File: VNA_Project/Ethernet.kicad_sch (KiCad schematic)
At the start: 0 parts

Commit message: minor changes eth
minor changes eth
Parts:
- added J1001: RJ45_Wuerth_7499010211A, Connector_RJ:RJ45_Wuerth_7499010211A_Horizontal, symbol Connector:RJ45_Wuerth_7499010211A
- added U1001: DP83848C, Package_QFP:LQFP-48_7x7mm_P0.5mm, symbol Interface_Ethernet:DP83848C
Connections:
- new net +3.3V: U1001.32 (IOVDD33), U1001.48 (IOVDD33)
- new net +3.3VA: U1001.22 (AVDD33)
- new net ETH_CRS_DV: U1001.40 (CRS/CRS_DV/LED_CFG)
- new net ETH_MDIO: U1001.30 (MDIO)
- new net ETH_RXD0: U1001.43 (RXD_0/PHY_AD1)
- new net ETH_RXD1: U1001.44 (RXD_1/PHY_AD2)
- new net ETH_RX_CLK: U1001.38 (RX_CLK)
- new net ETH_TXD0: U1001.3 (TXD_0)
- new net ETH_TXD1: U1001.4 (TXD_1)
- new net ETH_TX_EN: U1001.2 (TX_EN)
- new net GND: U1001.15 (AGND), U1001.19 (AGND), U1001.35 (IOGND), U1001.36 (DGND), U1001.47 (IOGND)
- new net NRST: U1001.29 (~{RESET})

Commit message: eth
eth
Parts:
- added C1001, C1002, C1004: 0.1u, symbol Device:C_Small
- added C1003: 10u, symbol Device:C_Small
- added C1005, C1006: 0.1u, symbol Device:C
- added D1001: RED, symbol Device:LED
- added D1002: GREEN, symbol Device:LED
- added D1003: BLUE, symbol Device:LED
- added FL1001, FL1002: Choke_CommonMode_PulseElectronics_PH9455x105NL, Inductor_THT:L_CommonMode_PulseElectronics_PH9455x105NL_1, symbol Filter:Choke_CommonMode_PulseElectronics_PH9455x105NL
- added R1001: 1.5k, symbol Device:R
- added R1002: 4.87k, symbol Device:R
- added R1003, R1004: 2.2k, symbol Device:R
- added R1005, R1006, R1007: 1k, symbol Device:R
- added R1008, R1009, R1010, R1011: 49.9, symbol Device:R
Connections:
- net +3.3V: now also C1005.1, C1006.1, R1001.1, R1008.2, R1009.1, R1010.2, R1011.1
- net +3.3VA: now also R1003.2, R1004.2
- net ETH_MDIO: now also R1001.2
- net GND: now also C1001.2, C1002.2, C1003.2, C1004.2, C1005.2, C1006.2, R1002.2, R1005.2, R1006.2, R1007.2
- net RD-: now reaches U1001.13 (RD-)
- net RD-: now also FL1002.2, R1011.2
- net RD+: now reaches U1001.14 (RD+)
- net RD+: now also FL1002.1, R1010.1
- net TD-: now reaches U1001.16 (TD-)
- net TD-: now also FL1001.2, R1009.2
- net TD+: now reaches U1001.17 (TD+)
- net TD+: now also FL1001.1, R1008.1
- net at U1001.18 (PFBIN1): now also U1001.23 (PFBOUT), U1001.37 (PFBIN2), C1001.1, C1002.1, C1003.1, C1004.1
- net at U1001.20 (RESERVED): now also R1003.1
- net at U1001.21 (RESERVED): now also R1004.1
- net at U1001.24 (RBIAS): now also R1002.1
- net LED_ACT: now reaches U1001.26 (AN_EN/LED_ACT/COL)
- net LED_ACT: now also D1003.2 (A)
- net LED_SPEED: now reaches U1001.27 (AN1/LED_SPEED)
- net LED_SPEED: now also D1002.2 (A)
- net LED_LINK: now reaches U1001.28 (AN0/LED_LINK)
- net LED_LINK: now also D1001.2 (A)
- new net: D1001.1 (K), R1005.1
- new net: D1002.1 (K), R1006.1
- new net: D1003.1 (K), R1007.1
- no-connect marks 0 -> 2
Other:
- note added: "1%"
- note added: "RMII Mode"
- note added: "Status LEDs"
- note added: "tantalum"
- moved on the sheet: J1001, U1001

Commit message: Eth done
Eth done
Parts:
- removed C1001, C1002, C1004: 0.1u, symbol Device:C_Small
- removed C1003: 10u, symbol Device:C_Small
- removed C1005, C1006: 0.1u, symbol Device:C
- removed D1001: RED, symbol Device:LED
- removed D1002: GREEN, symbol Device:LED
- removed D1003: BLUE, symbol Device:LED
- removed FL1001, FL1002: Choke_CommonMode_PulseElectronics_PH9455x105NL, Inductor_THT:L_CommonMode_PulseElectronics_PH9455x105NL_1, symbol Filter:Choke_CommonMode_PulseElectronics_PH9455x105NL
- removed R1001: 1.5k, symbol Device:R
- removed R1002: 4.87k, symbol Device:R
- removed R1003, R1004: 2.2k, symbol Device:R
- removed R1005, R1006, R1007: 1k, symbol Device:R
- removed R1008, R1009, R1010, R1011: 49.9, symbol Device:R
- removed U1001: DP83848C, Package_QFP:LQFP-48_7x7mm_P0.5mm, symbol Interface_Ethernet:DP83848C
- added C1, C10, C11, C7, C8, C9: 100n, symbol Device:C
- added C2, C3: 5.6p, symbol Device:C
- added C4: 1u, symbol Device:C
- added C5: 470p, symbol Device:C
- added C6: 10u, symbol Device:C
- added L1: 600R @ 100 MHz, symbol Device:L
- added R1: 0, symbol Device:R
- added R10, R12: 270, symbol Device:R
- added R11: 10K, symbol Device:R
- added R13, R14: 33, symbol Device:R_Small
- added R15: 10k, symbol Device:R_Small
- added R16: 12.1k, symbol Device:R_Small
- added R2, R3, R4, R7: 49.9, symbol Device:R
- added TR1: Wuerth_749013011A, Transformer_SMD:Transformer_Ethernet_Wuerth_749013011A, symbol Transformer:Wuerth_749013011A
- added U1: LAN8742A, Package_DFN_QFN:VQFN-24-1EP_4x4mm_P0.5mm_EP2.5x2.5mm_ThermalVias, symbol Interface_Ethernet:LAN8742A
- added U2: USBLC6-4SC6, Package_TO_SOT_SMD:SOT-23-6, symbol Power_Protection:USBLC6-4SC6
- added Y1: NX2016SA25MHz, symbol Device:Crystal_GND24
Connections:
- net +3.3V: now also C1.1, U1.9 (VDDIO)
- net +3.3VA: now also L1.1
- net ETH_CRS_DV: now also U1.11 (CRS_DV/MODE2)
- net ETH_MDIO: now also U1.12 (MDIO)
- net ETH_RXD0: now also R13.1
- net ETH_RXD1: now also R14.1
- net ETH_RX_CLK: now also U1.14 (~{INT}/REFCLKO)
- net ETH_TXD0: now also U1.17 (TXD0)
- net ETH_TXD1: now also U1.18 (TXD1)
- net ETH_TX_EN: now also U1.16 (TXEN)
- net GND: now also J1001.8, J1001.SH, C1.2, C10.2, C11.2, C2.2, C3.2, C4.2, C5.2, C6.2, C7.2, C8.2, C9.2, R10.2, R11.2, R12.2, R15.2, R16.1, U1.25 (VSS), U2.2 (GND), Y1.2, Y1.4
- net NRST: now also U1.15 (~{RST})
- net RD+: now also J1001.3 (RD+), TR1.11 (RX+)
- net RD-: now also J1001.6 (RD-), TR1.9 (RX-)
- net TD+: now also J1001.1 (TD+), TR1.16 (TX+)
- net TD-: now also J1001.2 (TD-), TR1.14 (TX-)
- net at J1001.10: now also R10.1
- net at J1001.11: now also R12.1
- net LED_REGOFF: now reaches J1001.12
- net LED_REGOFF: now also U1.3 (LED1/REGOFF)
- net CRD: now reaches J1001.4 (CTD)
- net CRD: now also TR1.10 (C_RX)
- net CTD: now reaches J1001.5 (CRD)
- net CTD: now also TR1.15 (C_TX)
- net LED_INTSEL: now reaches J1001.9
- net LED_INTSEL: now also R11.1, U1.2 (LED2/~{INTSEL})
- new net: R13.2, U1.8 (RXD0/MODE0)
- new net: R15.1, U1.10 (RXER/PHYAD0)
- new net: R16.2, U1.24 (RBIAS)
- new net: C2.1, R1.1, U1.5 (XTAL1/CLKIN)
- new net: C4.1, C5.1, U1.6 (VDDCR)
- new net: R14.2, U1.7 (RXD1/MODE1)
- new net: R1.2, Y1.1
- new net CT: C10.1, C11.1, C6.1, C7.1, C8.1, C9.1, L1.2, R2.1, R3.1, R4.1, R7.1, TR1.2 (C_TD), TR1.7 (C_RD), U1.1 (VDD2A), U1.19 (VDD1A), U2.5 (VBUS)
- new net ETH_MDC: U1.13 (MDC)
- new net RX+: R4.2, TR1.6 (RD+), U1.23 (RXP), U2.1 (I/O1)
- new net RX-: R7.2, TR1.8 (RD-), U1.22 (RXN), U2.6 (I/O4)
- new net TX+: R2.2, TR1.1 (TD+), U1.21 (TXP), U2.3 (I/O2)
- new net TX-: R3.2, TR1.3 (TD-), U1.20 (TXN), U2.4 (I/O3)
- new net xtal2_eth: C3.1, U1.4 (XTAL2), Y1.3
- no-connect marks 2 -> 0
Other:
- note added: "25MHZ"
- note added: "Connector"
- note added: "ESD"
- note added: "MAGNETICS"
- note added: "PHY"
- note removed: "1%"
- note removed: "Status LEDs"
- note removed: "tantalum"
- moved on the sheet: J1001

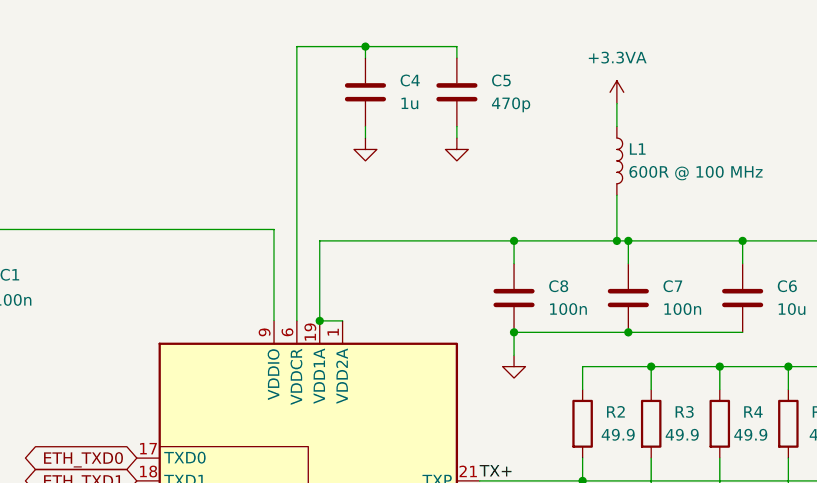
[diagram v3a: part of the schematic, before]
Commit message: finishing up front end
refining Non RF front end
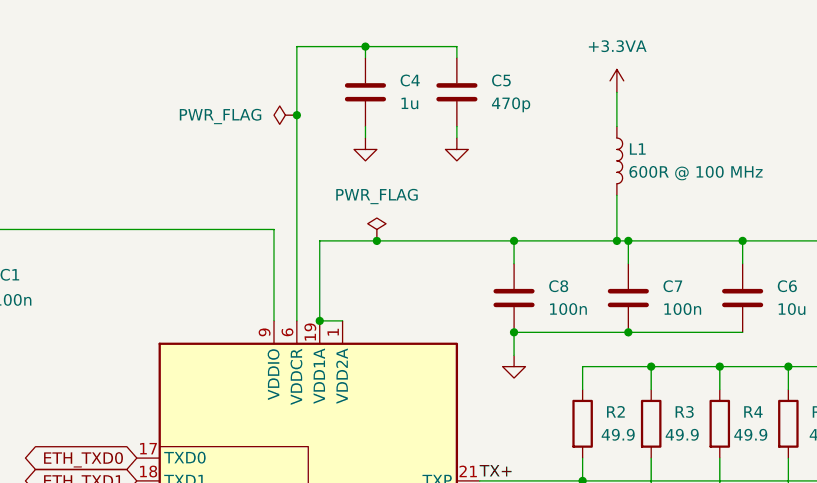
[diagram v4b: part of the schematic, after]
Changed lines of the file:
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@@
 	)
 	(junction
+		(at 125.73 22.86)
+		(diameter 0)
+		(color 0 0 0 0)
+	)
+	(junction
 		(at 162.56 36.83)
 		(diameter 0)
@@
 	)
 	(junction
+		(at 134.62 36.83)
+		(diameter 0)
+		(color 0 0 0 0)
+	)
+	(junction
 		(at 165.1 50.8)
 		(diameter 0)
@@
 	(wire
 		(pts
+			(xy 134.62 36.83) (xy 128.27 36.83)
+		)
+		(stroke
+			(width 0)
+			(type default)
+		)
+	)
+	(wire
+		(pts
 			(xy 226.06 140.97) (xy 251.46 140.97)
 		)
@@
 	(wire
 		(pts
+			(xy 125.73 22.86) (xy 125.73 45.72)
+		)
+		(stroke
+			(width 0)
+			(type default)
+		)
+	)
+	(wire
+		(pts
 			(xy 175.26 36.83) (xy 175.26 39.37)
 		)
@@
 	(wire
 		(pts
-			(xy 149.86 36.83) (xy 128.27 36.83)
+			(xy 149.86 36.83) (xy 134.62 36.83)
 		)
 		(stroke
@@
 	(wire
 		(pts
-			(xy 125.73 15.24) (xy 125.73 45.72)
+			(xy 125.73 15.24) (xy 125.73 22.86)
 		)
 		(stroke
@@
 	(wire
 		(pts
-			(xy 161.29 21.59) (xy 161.29 24.13)
+			(xy 161.29 20.32) (xy 161.29 24.13)
 		)
 		(stroke
@@
 	)
 	(symbol
+		(lib_id "power:PWR_FLAG")
+		(at 134.62 36.83 0)
+		(unit 1)
+		(exclude_from_sim no)
+		(in_bom yes)
+		(on_board yes)
+		(dnp no)
+		(fields_autoplaced yes)
+		(property "Reference" "#FLG08"
+			(at 134.62 34.925 0)
+			(effects
+				(font
+					(size 1.27 1.27)
+				)
+				(hide yes)
+			)
+		)
+		(property "Value" "PWR_FLAG"
+			(at 134.62 31.75 0)
+			(effects
+				(font
+					(size 1.27 1.27)
+				)
+			)
+		)
+		(property "Footprint" ""
+			(at 134.62 36.83 0)
+			(effects
+				(font
+					(size 1.27 1.27)
+				)
+				(hide yes)
+			)
+		)
+		(property "Datasheet" "~"
+			(at 134.62 36.83 0)
+			(effects
+				(font
+					(size 1.27 1.27)
+				)
+				(hide yes)
+			)
+		)
+		(property "Description" "Special symbol for telling ERC where power comes from"
+			(at 134.62 36.83 0)
+			(effects
+				(font
+					(size 1.27 1.27)
+				)
+				(hide yes)
+			)
+		)
+		(pin "1"
+		)
+		(instances
+			(project ""
+				(path "/8b9c6944-c5f7-4a92-a452-dc4fa5f3924d/76256ba9-bc22-4fd8-98b4-4441e825b7f8"
+					(reference "#FLG08")
+					(unit 1)
+				)
+			)
+		)
+	)
+	(symbol
 		(lib_id "power:GND")
 		(at 149.86 49.53 0)
@@
 	(symbol
 		(lib_id "power:+3.3VA")
-		(at 161.29 21.59 0)
+		(at 161.29 20.32 0)
 		(unit 1)
 		(exclude_from_sim no)
@@
 		(fields_autoplaced yes)
 		(property "Reference" "#PWR08"
-			(at 161.29 25.4 0)
+			(at 161.29 24.13 0)
 			(effects
 				(font
@@
 		)
 		(property "Value" "+3.3VA"
-			(at 161.29 16.51 0)
+			(at 161.29 15.24 0)
 			(effects
 				(font
@@
 		)
 		(property "Footprint" ""
-			(at 161.29 21.59 0)
+			(at 161.29 20.32 0)
 			(effects
 				(font
@@
 		)
 		(property "Datasheet" ""
-			(at 161.29 21.59 0)
+			(at 161.29 20.32 0)
 			(effects
 				(font
@@
 		)
 		(property "Description" "Power symbol creates a global label with name \"+3.3VA\""
-			(at 161.29 21.59 0)
+			(at 161.29 20.32 0)
 			(effects
 				(font
@@
 					(unit 1)
 				)
+			)
+		)
+	)
+	(symbol
+		(lib_id "power:PWR_FLAG")
+		(at 125.73 22.86 90)
+		(unit 1)
+		(exclude_from_sim no)
+		(in_bom yes)
+		(on_board yes)
+		(dnp no)
+		(fields_autoplaced yes)
+		(property "Reference" "#FLG09"
+			(at 123.825 22.86 0)
+			(effects
+				(font
+					(size 1.27 1.27)
+				)
+				(hide yes)
+			)
+		)
+		(property "Value" "PWR_FLAG"
+			(at 121.92 22.8599 90)
+			(effects
+				(font
+					(size 1.27 1.27)
+				)
+				(justify left)
+			)
+		)
+		(property "Footprint" ""
+			(at 125.73 22.86 0)
+			(effects
+				(font
+					(size 1.27 1.27)
+				)
+				(hide yes)
+			)
+		)
+		(property "Datasheet" "~"
+			(at 125.73 22.86 0)
+			(effects
+				(font
+					(size 1.27 1.27)
+				)
+				(hide yes)
+			)
+		)
+		(property "Description" "Special symbol for telling ERC where power comes from"
+			(at 125.73 22.86 0)
+			(effects
+				(font
+					(size 1.27 1.27)
+				)
+				(hide yes)
+			)
+		)
+		(pin "1"
+		)
+		(instances
+			(project "VNA_Project"
+				(path "/8b9c6944-c5f7-4a92-a452-dc4fa5f3924d/76256ba9-bc22-4fd8-98b4-4441e825b7f8"
+					(reference "#FLG09")
+					(unit 1)
+				)

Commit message: AA filtering
redoing AA filtering
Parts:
- added TP15, TP16: TestPoint, symbol Connector:TestPoint
- C2, C3: value 5.6p -> 10p
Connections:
- net +3.3V: now also TP15.1
- net CT: now also TP16.1
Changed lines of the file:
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@@
 	)
 	(junction
+		(at 128.27 41.91)
+		(diameter 0)
+		(color 0 0 0 0)
+	)
+	(junction
 		(at 218.44 149.86)
 		(diameter 0)
@@
 	)
 	(junction
+		(at 123.19 41.91)
+		(diameter 0)
+		(color 0 0 0 0)
+	)
+	(junction
 		(at 172.72 68.58)
 		(diameter 0)
@@
 	(wire
 		(pts
+			(xy 123.19 41.91) (xy 123.19 45.72)
+		)
+		(stroke
+			(width 0)
+			(type default)
+		)
+	)
+	(wire
+		(pts
 			(xy 157.48 63.5) (xy 157.48 83.82)
 		)
@@
 	(wire
 		(pts
-			(xy 123.19 35.56) (xy 123.19 45.72)
+			(xy 123.19 35.56) (xy 123.19 41.91)
 		)
 		(stroke
@@
 	(wire
 		(pts
-			(xy 157.48 83.82) (xy 203.2 83.82)
-		)
-		(stroke
-			(width 0)
-			(type default)
-		)
-	)
-	(wire
-		(pts
 			(xy 194.31 58.42) (xy 198.12 58.42)
 		)
@@
 	(wire
 		(pts
+			(xy 180.34 99.06) (xy 203.2 99.06)
+		)
+		(stroke
+			(width 0)
+			(type default)
+		)
+	)
+	(wire
+		(pts
 			(xy 196.85 106.68) (xy 196.85 107.95)
 		)
@@
 	(wire
 		(pts
+			(xy 172.72 93.98) (xy 203.2 93.98)
+		)
+		(stroke
+			(width 0)
+			(type default)
+		)
+	)
+	(wire
+		(pts
 			(xy 157.48 50.8) (xy 157.48 53.34)
 		)
@@
 	(wire
 		(pts
-			(xy 128.27 36.83) (xy 128.27 45.72)
+			(xy 128.27 36.83) (xy 128.27 41.91)
 		)
 		(stroke
@@
 	(wire
 		(pts
+			(xy 85.09 93.98) (xy 107.95 93.98)
+		)
+		(stroke
+			(width 0)
+			(type default)
+		)
+	)
+	(wire
+		(pts
 			(xy 146.05 86.36) (xy 146.05 100.33)
 		)
@@
 	(wire
 		(pts
-			(xy 85.09 93.98) (xy 107.95 93.98)
-		)
-		(stroke
-			(width 0)
-			(type default)
-		)
-	)
-	(wire
-		(pts
 			(xy 196.85 60.96) (xy 198.12 60.96)
 		)
@@
 	(wire
 		(pts
+			(xy 157.48 83.82) (xy 203.2 83.82)
+		)
+		(stroke
+			(width 0)
+			(type default)
+		)
+	)
+	(wire
+		(pts
 			(xy 88.9 34.29) (xy 88.9 35.56)
 		)
@@
 	(wire
 		(pts
-			(xy 172.72 93.98) (xy 203.2 93.98)
-		)
-		(stroke
-			(width 0)
-			(type default)
-		)
-	)
-	(wire
-		(pts
 			(xy 196.85 71.12) (xy 196.85 60.96)
 		)
@@
 	(wire
 		(pts
-			(xy 179.07 138.43) (xy 182.88 138.43)
+			(xy 128.27 41.91) (xy 128.27 45.72)
 		)
 		(stroke
@@
 	(wire
 		(pts
-			(xy 180.34 99.06) (xy 203.2 99.06)
+			(xy 179.07 138.43) (xy 182.88 138.43)
 		)
 		(stroke
@@
 	)
 	(symbol
+		(lib_id "Connector:TestPoint")
+		(at 128.27 41.91 270)
+		(unit 1)
+		(exclude_from_sim no)
+		(in_bom yes)
+		(on_board yes)
+		(dnp no)
+		(fields_autoplaced yes)
+		(property "Reference" "TP16"
+			(at 133.35 41.9099 90)
+			(effects
+				(font
+					(size 1.27 1.27)
+				)
+				(justify left)
+			)
+		)
+		(property "Value" "TestPoint"
+			(at 133.35 43.1799 90)
+			(effects
+				(font
+					(size 1.27 1.27)
+				)
+				(justify left)
+				(hide yes)
+			)
+		)
+		(property "Footprint" ""
+			(at 128.27 46.99 0)
+			(effects
+				(font
+					(size 1.27 1.27)
+				)
+				(hide yes)
+			)
+		)
+		(property "Datasheet" "~"
+			(at 128.27 46.99 0)
+			(effects
+				(font
+					(size 1.27 1.27)
+				)
+				(hide yes)
+			)
+		)
+		(property "Description" "test point"
+			(at 128.27 41.91 0)
+			(effects
+				(font
+					(size 1.27 1.27)
+				)
+				(hide yes)
+			)
+		)
+		(pin "1"
+		)
+		(instances
+			(project "VNA_Project"
+				(path "/8b9c6944-c5f7-4a92-a452-dc4fa5f3924d/76256ba9-bc22-4fd8-98b4-4441e825b7f8"
+					(reference "TP16")
+					(unit 1)
+				)
+			)
+		)
+	)
+	(symbol
 		(lib_id "Device:C")
 		(at 175.26 43.18 0)
@@
 	)
 	(symbol
+		(lib_id "Connector:TestPoint")
+		(at 123.19 41.91 90)
+		(unit 1)
+		(exclude_from_sim no)
+		(in_bom yes)
+		(on_board yes)
+		(dnp no)
+		(fields_autoplaced yes)
+		(property "Reference" "TP15"
+			(at 119.888 39.37 90)
+			(effects
+				(font
+					(size 1.27 1.27)
+				)
+			)
+		)
+		(property "Value" "TestPoint"
+			(at 118.11 40.6401 90)
+			(effects
+				(font
+					(size 1.27 1.27)
+				)
+				(justify left)
+				(hide yes)
+			)
+		)
+		(property "Footprint" ""
+			(at 123.19 36.83 0)
+			(effects
+				(font
+					(size 1.27 1.27)
+				)
+				(hide yes)
+			)
+		)
+		(property "Datasheet" "~"
+			(at 123.19 36.83 0)
+			(effects
+				(font
+					(size 1.27 1.27)
+				)
+				(hide yes)
+			)
+		)
+		(property "Description" "test point"
+			(at 123.19 41.91 0)
+			(effects
+				(font
+					(size 1.27 1.27)
+				)
+				(hide yes)
+			)
+		)
+		(pin "1"
+		)
+		(instances
+			(project "VNA_Project"
+				(path "/8b9c6944-c5f7-4a92-a452-dc4fa5f3924d/76256ba9-bc22-4fd8-98b4-4441e825b7f8"
+					(reference "TP15")
+					(unit 1)
+				)
+			)
+		)
+	)
+	(symbol
 		(lib_id "Device:C")
 		(at 182.88 111.76 0)
@@
 		(fields_autoplaced yes)
 		(property "Reference" "C3"
-			(at 36.83 100.3299 0)
+			(at 44.45 100.3299 0)
 			(effects
 				(font
 					(size 1.27 1.27)
 				)
-				(justify left)
+				(justify right)
 			)
 		)
-		(property "Value" "5.6p"
-			(at 36.83 102.8699 0)
+		(property "Value" "10p"
+			(at 44.45 102.8699 0)
 			(effects
 				(font
 					(size 1.27 1.27)
 				)
-				(justify left)
+				(justify right)
 			)
 		)
@@
 		(fields_autoplaced yes)
 		(property "Reference" "C2"
-			(at 81.28 100.3299 0)
+			(at 88.9 100.3299 0)
 			(effects
 				(font
 					(size 1.27 1.27)
 				)
-				(justify left)
+				(justify right)
 			)
 		)
-		(property "Value" "5.6p"
-			(at 81.28 102.8699 0)
+		(property "Value" "10p"
+			(at 88.9 102.8699 0)
 			(effects
 				(font
 					(size 1.27 1.27)
 				)
-				(justify left)
+				(justify right)
 			)
 		)

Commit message: footprints + initial layout shape
footprints + initial layout shape
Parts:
- C501: renamed from C3; footprint (none) -> Capacitor_SMD:C_0603_1608Metric_Pad1.08x0.95mm_HandSolder
- C502: renamed from C2; footprint (none) -> Capacitor_SMD:C_0603_1608Metric_Pad1.08x0.95mm_HandSolder
- C503: renamed from C1; footprint (none) -> Capacitor_SMD:C_0603_1608Metric_Pad1.08x0.95mm_HandSolder
- C504: renamed from C4; footprint (none) -> Capacitor_SMD:C_0603_1608Metric_Pad1.08x0.95mm_HandSolder
- C505: renamed from C5; footprint (none) -> Capacitor_SMD:C_0603_1608Metric_Pad1.08x0.95mm_HandSolder
- C506: renamed from C8; footprint (none) -> Capacitor_SMD:C_0603_1608Metric_Pad1.08x0.95mm_HandSolder
- C507: renamed from C7; footprint (none) -> Capacitor_SMD:C_0603_1608Metric_Pad1.08x0.95mm_HandSolder
- C508: renamed from C6; footprint (none) -> Capacitor_SMD:C_0603_1608Metric_Pad1.08x0.95mm_HandSolder
- C509: renamed from C10; footprint (none) -> Capacitor_SMD:C_0603_1608Metric_Pad1.08x0.95mm_HandSolder
- C510: renamed from C11; footprint (none) -> Capacitor_SMD:C_0603_1608Metric_Pad1.08x0.95mm_HandSolder
- C511: renamed from C9; footprint (none) -> Capacitor_SMD:C_0603_1608Metric_Pad1.08x0.95mm_HandSolder
- L501: renamed from L1; footprint (none) -> Inductor_SMD:L_0805_2012Metric_Pad1.15x1.40mm_HandSolder
- R501: renamed from R1; footprint (none) -> Resistor_SMD:R_0603_1608Metric_Pad0.98x0.95mm_HandSolder
- R502: renamed from R13; footprint (none) -> Resistor_SMD:R_0603_1608Metric_Pad0.98x0.95mm_HandSolder
- R503: renamed from R14; footprint (none) -> Resistor_SMD:R_0603_1608Metric_Pad0.98x0.95mm_HandSolder
- R504: renamed from R15; footprint (none) -> Resistor_SMD:R_0603_1608Metric_Pad0.98x0.95mm_HandSolder
- R505: renamed from R16; footprint (none) -> Resistor_SMD:R_0603_1608Metric_Pad0.98x0.95mm_HandSolder
- R506: renamed from R2; footprint (none) -> Resistor_SMD:R_0603_1608Metric_Pad0.98x0.95mm_HandSolder
- R507: renamed from R3; footprint (none) -> Resistor_SMD:R_0603_1608Metric_Pad0.98x0.95mm_HandSolder
- R508: renamed from R4; footprint (none) -> Resistor_SMD:R_0603_1608Metric_Pad0.98x0.95mm_HandSolder
- R509: renamed from R7; footprint (none) -> Resistor_SMD:R_0603_1608Metric_Pad0.98x0.95mm_HandSolder
- R510: renamed from R10; footprint (none) -> Resistor_SMD:R_0603_1608Metric_Pad0.98x0.95mm_HandSolder
- R511: renamed from R12; footprint (none) -> Resistor_SMD:R_0603_1608Metric_Pad0.98x0.95mm_HandSolder
- R512: renamed from R11; footprint (none) -> Resistor_SMD:R_0603_1608Metric_Pad0.98x0.95mm_HandSolder
- TP501: renamed from TP15; footprint (none) -> TestPoint:TestPoint_Pad_D4.0mm
- TP502: renamed from TP16; footprint (none) -> TestPoint:TestPoint_Pad_D4.0mm
- U501: renamed from U1; footprint Package_DFN_QFN:VQFN-24-1EP_4x4mm_P0.5mm_EP2.5x2.5mm_ThermalVias -> Package_DFN_QFN:VQFN-24-1EP_4x4mm_P0.5mm_EP2.5x2.5mm
- U502: renamed from U2; footprint Package_TO_SOT_SMD:SOT-23-6 -> Package_TO_SOT_SMD:SOT-23-6_Handsoldering
- Y501: renamed from Y1; value NX2016SA25MHz -> STDCZS1-25M; footprint (none) -> Crystal:Crystal_SMD_2016-4Pin_2.0x1.6mm
- renumbered J1001 to J501, TR1 to TR501

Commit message: Layout
Layout
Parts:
- removed J501: RJ45_Wuerth_7499010211A, Connector_RJ:RJ45_Wuerth_7499010211A_Horizontal, symbol Connector:RJ45_Wuerth_7499010211A
- removed R510, R511: 270, Resistor_SMD:R_0603_1608Metric_Pad0.98x0.95mm_HandSolder, symbol Device:R
- removed R512: 10K, Resistor_SMD:R_0603_1608Metric_Pad0.98x0.95mm_HandSolder, symbol Device:R
- added J502: 8P8C_LED_Shielded_x2, Connector_RJ:RJ45_Wuerth_7499010211A_Horizontal, symbol Connector:8P8C_LED_Shielded_x2
- added R513, R514: 270, Resistor_SMD:R_0603_1608Metric_Pad0.98x0.95mm_HandSolder, symbol Device:R
- added R515: 10K, Resistor_SMD:R_0603_1608Metric_Pad0.98x0.95mm_HandSolder, symbol Device:R
- added SW501: SW_SPDT, Button_Switch_THT:SW_Slide_SPDT_Straight_CK_OS102011MS2Q, symbol Switch:SW_SPDT
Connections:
- net CRD: now also J502.4
- net CTD: now also J502.5
- net GND: now also J502.8, J502.SH, R513.2, R514.2, R515.2, SW501.3 (C)
- net LED_INTSEL: now also J502.10, R515.1
- net LED_REGOFF: now also J502.12
- net RD+: now also J502.3
- net RD-: now also J502.6
- net TD+: now also J502.1
- net TD-: now also J502.2
- new net: J502.9, R513.1
- new net: J502.7, SW501.2 (B)
- new net: J502.11, R514.1
- no-connect marks 0 -> 1
